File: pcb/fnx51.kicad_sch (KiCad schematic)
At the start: 10 parts, among them U1 AT89C51ED2-SMSUM

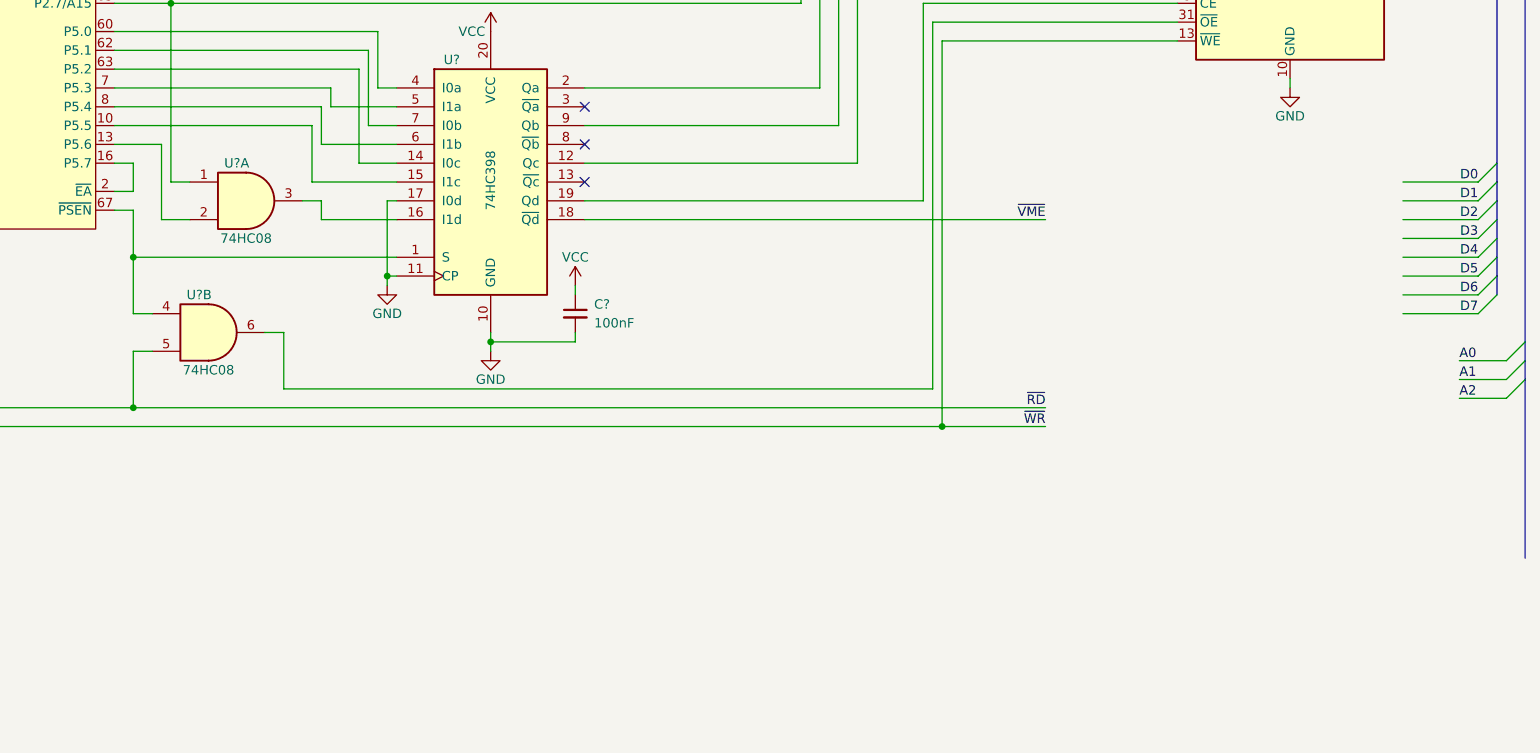
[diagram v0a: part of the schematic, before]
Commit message: add hierarchical schematic for video hardware
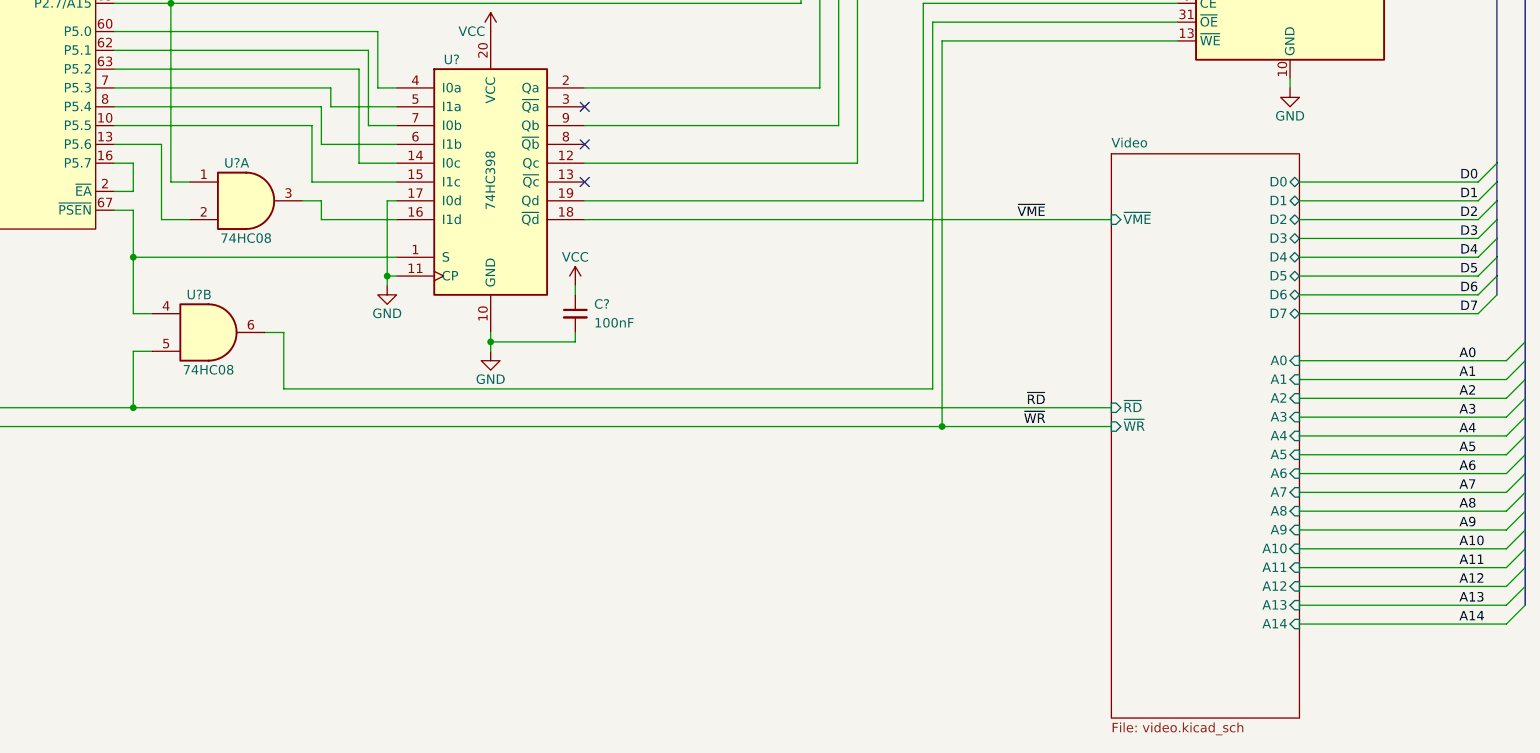
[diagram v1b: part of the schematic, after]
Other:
- added sheet Video (video.kicad_sch)

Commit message: WIP
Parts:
- removed U?: 74HC398, symbol 74xx:74LS398
- removed U?: IS61C5128AL-10KLI, Package_SO:SOJ-36_10.16x23.49mm_P1.27mm, symbol Memory_RAM:IS61C5128AL-10KLI
- added U12: AS6C4008-55PCN, Package_DIP:DIP-32_W15.24mm, symbol Memory_RAM:AS6C4008-55PCN
- added U4: 74HC04, symbol 74xx:74HC04
- added U5: 74HC157, symbol 74xx:74LS157
- gave numbers to parts that had none: 6
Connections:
- net A0: now also U12.12 (A0)
- net A1: now also U12.11 (A1)
- net A10: now also U12.23 (A10)
- net A11: now also U12.25 (A11)
- net A12: now also U12.4 (A12)
- net A13: now also U12.28 (A13)
- net A14: now also U12.3 (A14)
- net A15: now also U12.31 (A15)
- net A16: now also U12.2 (A16), U5.4 (Za)
- net A17: now also U12.30 (A17), U5.7 (Zb)
- net A18: now also U12.1 (A18), U5.9 (Zc)
- net A2: now also U12.10 (A2)
- net A3: now also U12.9 (A3)
- net A4: now also U12.8 (A4)
- net A5: now also U12.7 (A5)
- net A6: now also U12.6 (A6)
- net A7: now also U12.5 (A7)
- net A8: now also U12.27 (A8)
- net A9: now also U12.26 (A9)
- net D0: now also U12.13 (DQ0)
- net D1: now also U12.14 (DQ1)
- net D2: now also U12.15 (DQ2)
- net D3: now also U12.17 (DQ3)
- net D4: now also U12.18 (DQ4)
- net D5: now also U12.19 (DQ5)
- net D6: now also U12.20 (DQ6)
- net D7: now also U12.21 (DQ7)
- net GND: now also U12.16 (VSS), U5.14 (I0d), U5.15 (E), U5.8 (GND)
- net VCC: now also U12.32 (VCC), U5.16 (VCC)
- net ~{VME}: now also U4.2
- net ~{WR}: now also U12.29 (WE#)
- net at U1.67 (~{PSEN}), U2.4: now also U5.1 (S)
- net at U1.63 (P5.2): now also U5.11 (I0c)
- net at U1.10 (P5.5): now also U5.10 (I1c)
- net at U2.3: now also U5.13 (I1d)
- net at U1.60 (P5.0): now also U5.2 (I0a)
- net at U1.7 (P5.3): now also U5.3 (I1a)
- net at U1.8 (P5.4): now also U5.6 (I1b)
- net at U1.62 (P5.1): now also U5.5 (I0b)
- net at U2.6: now also U12.24 (OE#)
- new net: U12.22 (CE#), U4.1, U5.12 (Zd)
- no-connect marks 3 -> 0
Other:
- moved on the sheet: C1, C2, C3, C4, U1, U2A, U2B, U3

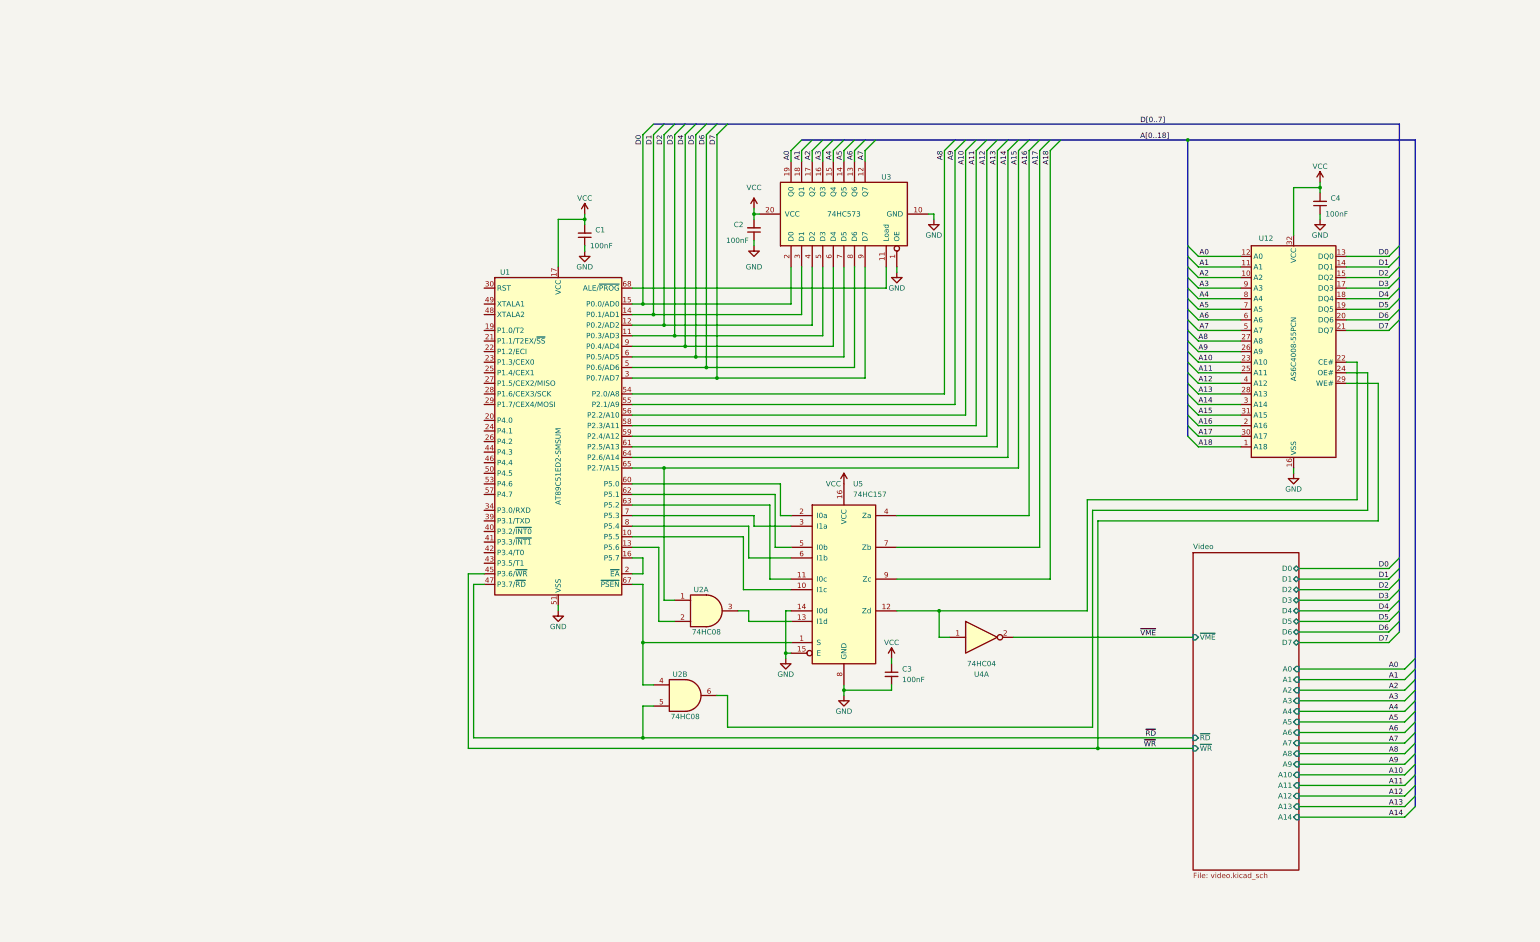
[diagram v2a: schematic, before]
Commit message: schematic: video signals, address counter, extra registers
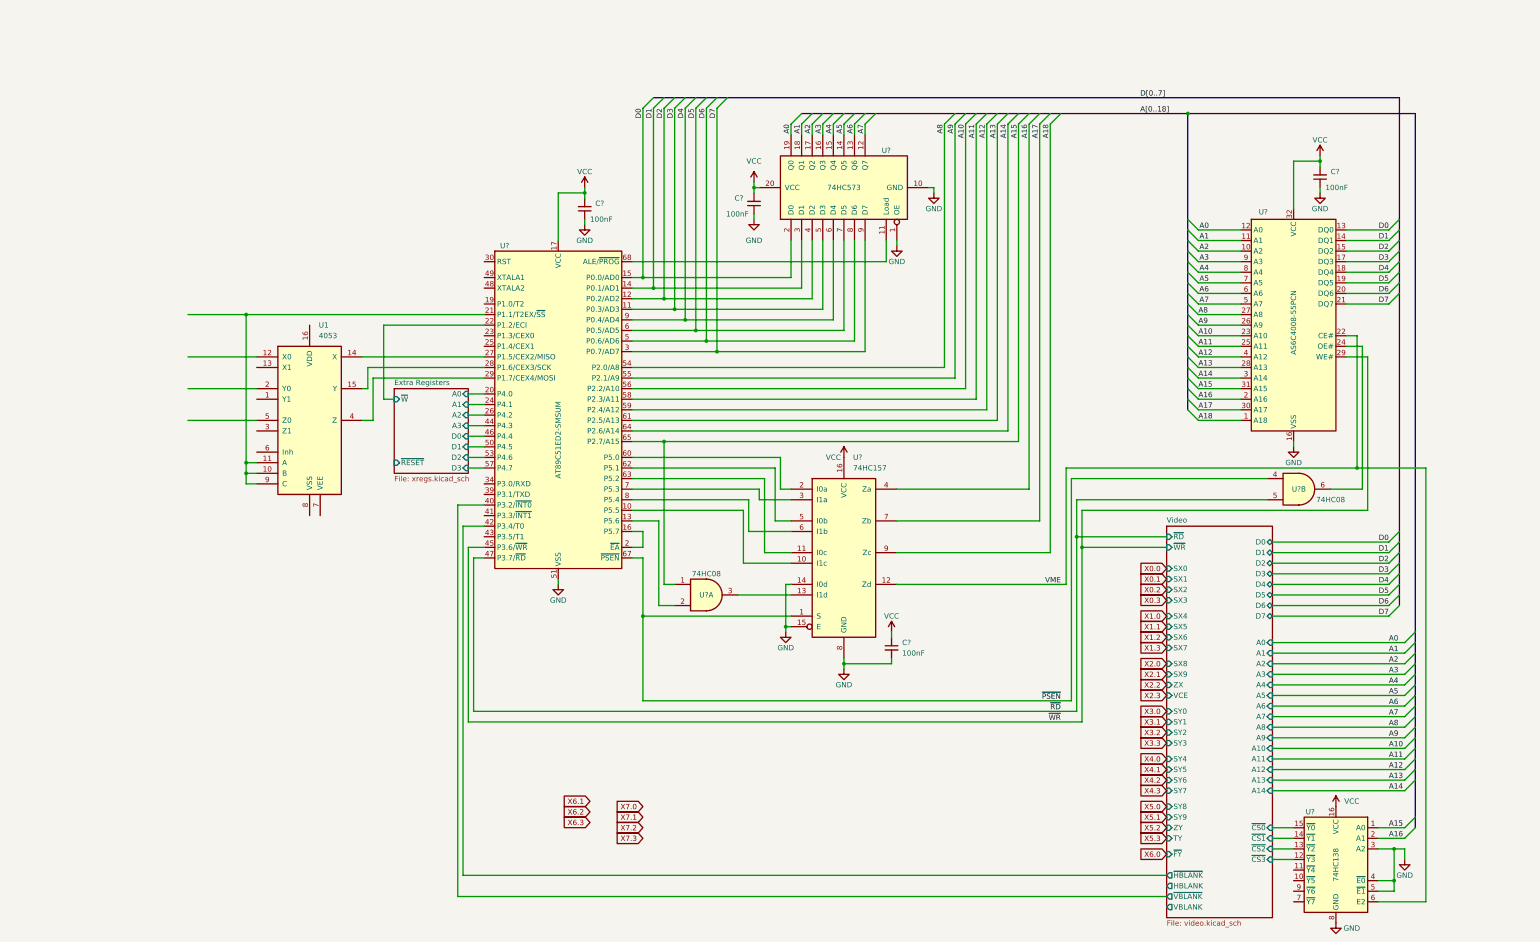
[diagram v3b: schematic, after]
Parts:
- removed U4: 74HC04, symbol 74xx:74HC04
- added U1: 4053, symbol 4xxx:4053
- added U?: 74HC138, symbol 74xx:74HC138
- renumbered C4 to C?, C2 to C?, C1 to C?, C3 to C?, U1 to U?, U12 to U?, U3 to U?, U2 to U?, U5 to U?
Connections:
- net A15: now also U?.1 (A0)
- net A16: now also U?.2 (A1)
- net GND: now also U?.3 (A2), U?.4 (~{E0}), U?.5 (~{E1}), U?.8 (GND)
- net VCC: now also U?.16 (VCC)
- net Extra Registers/A0: now reaches U?.20 (P4.0)
- net at U?.21 (P1.1/T2EX/~{SS}): now also U1.10 (B), U1.11 (A), U1.9 (C)
- net Extra Registers/~{W}: now reaches U?.22 (P1.2/ECI)
- net Extra Registers/A1: now reaches U?.24 (P4.1)
- net Extra Registers/A2: now reaches U?.26 (P4.2)
- net at U?.27 (P1.5/CEX2/MISO): now also U1.14 (X)
- net at U?.28 (P1.6/CEX3/SCK): now also U1.15 (Y)
- net at U?.29 (P1.7/CEX4/MOSI): now also U1.4 (Z)
- net Video/~{VBLANK}: now reaches U?.40 (P3.2/~{INT0})
- net Video/~{HBLANK}: now reaches U?.42 (P3.4/T0)
- net Extra Registers/A3: now reaches U?.44 (P4.3)
- net Extra Registers/D0: now reaches U?.46 (P4.4)
- net Extra Registers/D1: now reaches U?.50 (P4.5)
- net Extra Registers/D2: now reaches U?.53 (P4.6)
- net Extra Registers/D3: now reaches U?.57 (P4.7)
- net ~{PSEN}: now reaches U?.1 (S), U?.4, U?.67 (~{PSEN})
- net VME: now reaches U?.12 (Zd), U?.22 (CE#)
- net VME: now also U?.6 (E2)
- new net Video/~{CS0}: U?.15 (~{Y0})
- new net Video/~{CS1}: U?.14 (~{Y1})
- new net Video/~{CS2}: U?.13 (~{Y2})
- new net Video/~{CS3}: U?.12 (~{Y3})
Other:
- added sheet Extra Registers (xregs.kicad_sch)
- sheet Video ports: added HBLANK, SX0, SX1, SX2, SX3, SX4, SX5, SX6, SX7, SX8, SX9, SY0, SY1, SY2, SY3, SY4, SY5, SY6, SY7, SY8, SY9, TY, VBLANK, VCE, ZX, ZY, ~{CS0}, ~{CS1}, ~{CS2}, ~{CS3}, ~{FY}, ~{HBLANK}, ~{VBLANK}; removed ~{VME}
- moved on the sheet: C?, U?, U?A, U?B

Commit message: WIP schematic
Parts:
- removed U?: 74HC157, symbol 74xx:74LS157
- removed U?: 74HC138, symbol 74xx:74HC138
- added J1: Screw_Terminal_01x10, symbol Connector:Screw_Terminal_01x10
- added J2: SPI0, symbol Connector_Generic:Conn_02x06_Odd_Even
- added J3: SPI1, symbol Connector_Generic:Conn_02x06_Odd_Even
- added U3: 74LS139, symbol 74xx:74LS139
- added U5: 4053, symbol 4xxx:4053
- added v: 74HC158, symbol 74xx:74LS158
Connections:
- net A16: now also v.4 (Za)
- net A17: now also v.7 (Zb)
- net A18: now also v.12 (Zc)
- net GND: now also U1.6 (Inh), U1.7 (VEE), U1.8 (VSS), J1.10 (Pin_10), J2.10 (Pin_10), J2.12 (Pin_12), J2.2 (Pin_2), J2.4 (Pin_4), J2.6 (Pin_6), J2.8 (Pin_8), J3.10 (Pin_10), J3.12 (Pin_12), J3.2 (Pin_2), J3.4 (Pin_4), J3.6 (Pin_6), J3.8 (Pin_8), U5.6 (Inh), U5.7 (VEE), U5.8 (VSS), v.11 (I0d), v.15 (E), v.8 (GND)
- net VCC: now also U1.16 (VDD), J2.1 (Pin_1), J3.1 (Pin_1), v.16 (VCC)
- net Video/~{HBLANK}: now also U?.19 (P1.0/T2); no longer U?.42 (P3.4/T0)
- net X6.3: now also U5.11 (A)
- net X7.0: now also J1.6 (Pin_6)
- net X7.1: now also J1.7 (Pin_7)
- net X7.2: now also J1.8 (Pin_8)
- net X7.3: now also J1.9 (Pin_9)
- net ~{PSEN}: now also v.1 (S)
- net at U?.10 (P5.5): now also v.13 (I1c)
- net Video/VMAP: now reaches U?.13 (P5.6), U?.2
- net MISO: now reaches U1.10 (B), U1.11 (A), U1.9 (C), U?.21 (P1.1/T2EX/~{SS})
- net MISO: now also U1.12 (X0), J2.7 (Pin_7), J3.7 (Pin_7), U3.1 (E), U5.10 (B), U5.9 (C)
- net at U?.23 (P1.3/CEX0): now also U5.15 (Y)
- net at U?.25 (P1.4/CEX1): now also U5.4 (Z)
- net RXD: now reaches U?.34 (P3.0/RXD)
- net TXD: now reaches U?.39 (P3.1/TXD)
- net ~{INT1}: now reaches U?.41 (P3.3/~{INT1})
- net ~{INT1}: now also U5.14 (X)
- net CTS: now reaches U?.43 (P3.5/T1)
- net at U?.60 (P5.0): now also v.2 (I0a)
- net at U?.62 (P5.1): now also v.5 (I0b)
- net at U?.63 (P5.2): now also v.14 (I0c)
- net at U?.7 (P5.3): now also v.3 (I1a)
- net at U?.8 (P5.4): now also v.6 (I1b)
- net at U?.3: now also v.10 (I1d)
- net PWM3: now reaches U1.1 (Y1)
- net PWM3: now also J1.4 (Pin_4)
- net PWM2: now reaches U1.13 (X1)
- net PWM2: now also J1.3 (Pin_3)
- net SCK: now reaches U1.2 (Y0)
- net SCK: now also J2.9 (Pin_9), J3.9 (Pin_9)
- net PWM4: now reaches U1.3 (Z1)
- net PWM4: now also J1.5 (Pin_5)
- net MOSI: now reaches U1.5 (Z0)
- net MOSI: now also J2.11 (Pin_11), J3.11 (Pin_11)
- net VME renamed ~{VME}
- net ~{VME}: now also v.9 (Zd)
- new net: U3.3 (A1), U5.2 (Y0)
- new net: U3.2 (A0), U5.5 (Z0)
- new net: J2.5 (Pin_5), U3.4 (O0)
- new net: J3.5 (Pin_5), U3.5 (O1)
- new net +3.3V: J2.3 (Pin_3), J3.3 (Pin_3)
- new net Ethernet/CS: U3.7 (O3)
- new net PWM0: J1.1 (Pin_1), U5.1 (Y1)
- new net PWM1: J1.2 (Pin_2), U5.3 (Z1)
- new net RTS: U?.42 (P3.4/T0)
- new net Video/~{SS}: U3.6 (O2)
- new net ~{CPINT}: U5.12 (X0)
- new net ~{ETHINT}: U5.13 (X1)
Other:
- added sheet Ethernet (ethernet.kicad_sch)
- sheet Video ports: added MISO, MOSI, SCK, VMAP, ~{CPIRQ}, ~{CPRST}, ~{SS}, ~{VME}; removed HBLANK, VBLANK, ~{CS0}, ~{CS1}, ~{CS2}, ~{CS3}
- moved on the sheet: C?, U1, U?, U?A, U?B

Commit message: WIP schematic
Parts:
- gave numbers to parts that had none: 8
- renumbered U3 to U1, U5 to U2, U1 to U3, v to U7
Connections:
- net VCC is gone; now on net +5V: C1.2, C2.2, C3.1, C4.2, J2.1 (Pin_1), J3.1 (Pin_1), U3.16 (VDD), U4.17 (VCC), U6.20 (VCC), U7.16 (VCC), U8.32 (VCC)
- net +5V: now reaches U2.16 (VDD)
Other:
- added sheet Audio (audio.kicad_sch)
- moved on the sheet: C1, C2, C3, C4, J1, J2, J3, U1A, U2, U3, U4, U5A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

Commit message: WIP PCB
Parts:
- added JP?: Jumper_2_Small_Bridged, symbol Jumper:Jumper_2_Small_Bridged
- renumbered C4 to C?, C2 to C?, C1 to C?, C3 to C?, J1 to J?, J3 to J?, J2 to J?, U4 to U?, U8 to U?, U2 to U?, U1 to U?, U7 to U?, U6 to U?, U5 to U?, U3 to U?
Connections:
- net at U?.16 (P5.7): now also JP?.1 (A); no longer U?.2 (~{EA})
- new net: JP?.2 (B), U?.2 (~{EA})
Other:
- sheet Audio ports: added D0, D1, D2, D3, D4, D5, D6, D7, DC3, FILTER0, FILTER1, FILTER2, FM12, LOAD0, LOAD1, LOAD2, LOAD3, MIX0, MIX1, MIX2, OCTAVE0, OCTAVE1, OCTAVE2, OCTAVE3, PWM0, PWM1, PWM2, PWM3, PWM4, WAVEFORM0, WAVEFORM1, WAVEFORM2, WAVEFORM3; removed none
- moved on the sheet: J?

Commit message: WIP PCB
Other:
- sheet Audio ports: added RESON0, RESON1, TUNE; removed none
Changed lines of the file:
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@@
 		)
 		(pin "DC3" input
-			(at 38.1 124.46 180)
+			(at 38.1 135.89 180)
 			(effects
 				(font
@@
 		)
 		(pin "FM12" input
-			(at 38.1 135.89 180)
+			(at 38.1 124.46 180)
 			(effects
 				(font
@@
 			)
 		)
+		(pin "RESON0" input
+			(at 38.1 139.7 180)
+			(effects
+				(font
+					(size 1.27 1.27)
+				)
+				(justify left)
+			)
+		)
+		(pin "RESON1" input
+			(at 38.1 142.24 180)
+			(effects
+				(font
+					(size 1.27 1.27)
+				)
+				(justify left)
+			)
+		)
+		(pin "TUNE" input
+			(at 38.1 144.78 180)
+			(effects
+				(font
+					(size 1.27 1.27)
+				)
+				(justify left)
+			)
+		)

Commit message: wip schematic
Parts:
- removed JP?: Jumper_2_Small_Bridged, symbol Jumper:Jumper_2_Small_Bridged
- added J?: Conn_01x03_Pin, symbol Connector:Conn_01x03_Pin
- added R? (x5): R, symbol Device:R
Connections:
- net +5V: now also J?.3 (Pin_3), R?.1, R?.1, R?.1, R?.1, R?.1
- net MISO: no longer U?.1 (E), U?.10 (B), U?.10 (B), U?.11 (A), U?.21 (P1.1/T2EX/~{SS}), U?.9 (C), U?.9 (C)
- net PWM0: now also R?.2
- net PWM1: now also R?.2
- net PWM2: now also R?.2
- net PWM3: now also R?.2
- net PWM4: now also R?.2
- net X6.2: now also U?.11 (A)
- net X6.3: no longer U?.11 (A)
- net at U?.16 (P5.7): now also J?.1 (Pin_1)
- net at U?.2 (~{EA}): now also J?.2 (Pin_2)
- new net: U?.1 (E), U?.10 (B), U?.10 (B), U?.11 (A), U?.21 (P1.1/T2EX/~{SS}), U?.9 (C), U?.9 (C)
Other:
- sheet Audio ports: added FLOAT; removed none
